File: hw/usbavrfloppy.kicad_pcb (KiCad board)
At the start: 2 copper layers, 96.5 x 70.5 mm, 67 parts, among them CON1 CONN_02X03, J1 bothdrv, J2 floppy_conn, J3 floppy_power, J5 USB_B, J6 PWRIN, J7 USB_OTG, P1 CONN_01X03, P2 CONN_01X01, P3 CONN_01X01, P4 CONN_01X01, P5 CONN_01X01, Q1 BSS138, Q10 BSS138, Q2 BSS138, Q3 BSS138, Q4 BSS138, Q5 BSS138, Q6 BSS138, Q7 BSS138, Q8 BSS138, Q9 BSS138, SW1 ~mRESET, U1 ATMEGA88-A, U2 FT232RL, Y1 16MHz

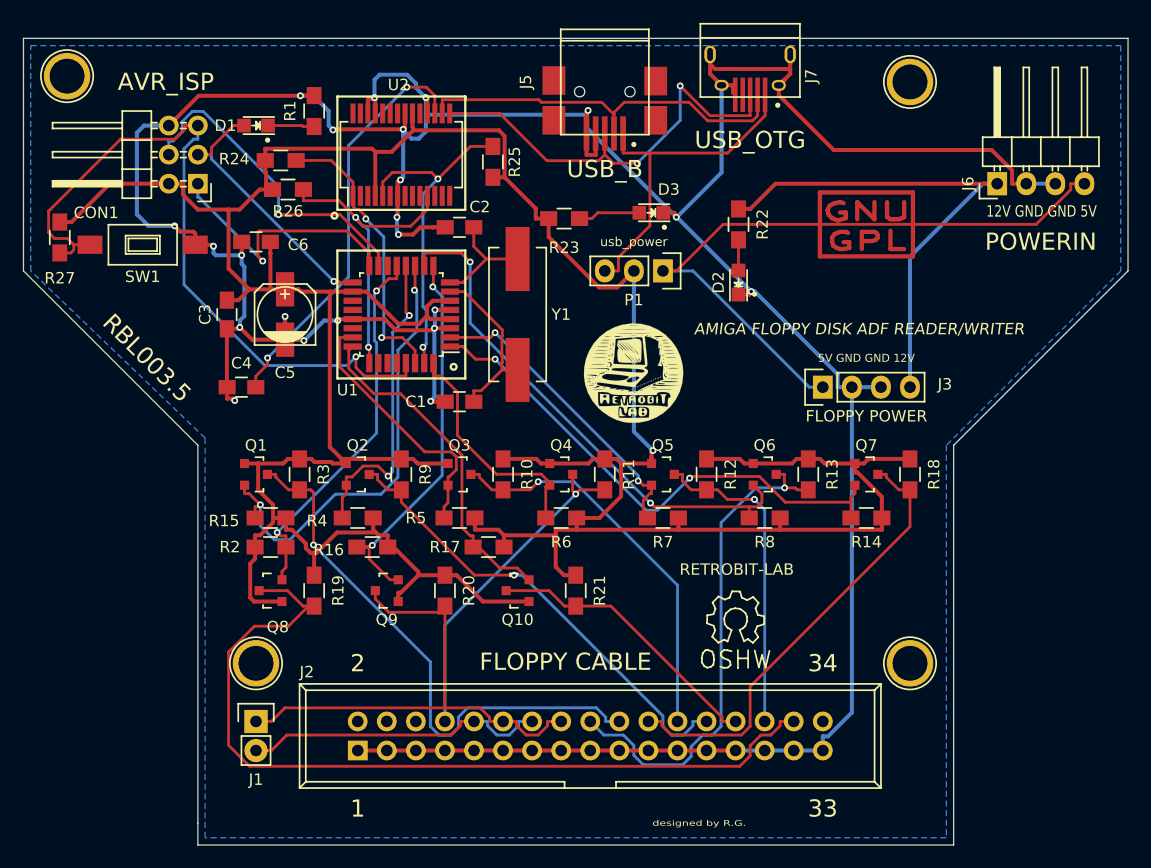
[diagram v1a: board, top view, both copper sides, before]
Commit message: Modified for new 3d components and logos
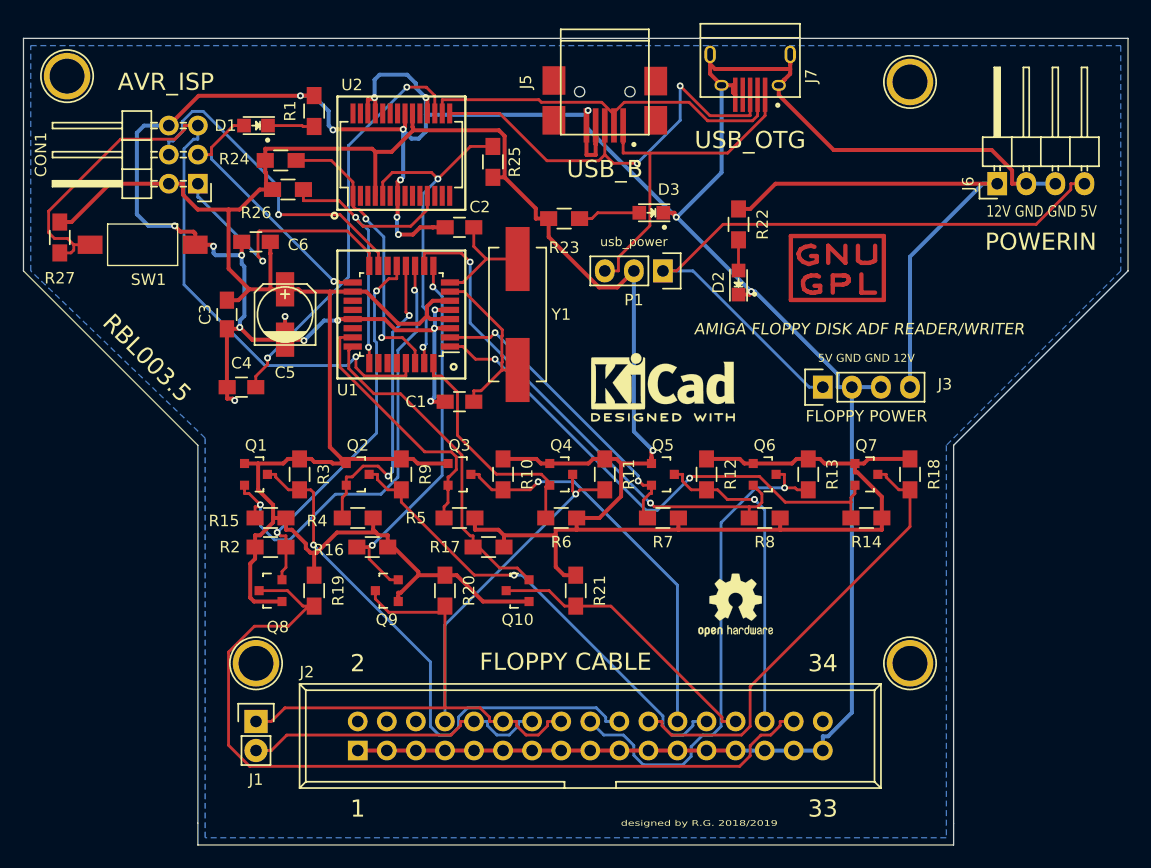
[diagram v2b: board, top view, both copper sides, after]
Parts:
- removed GNULOGO: Symbol_GNU-GPL_CopperTop_Small, Symbols:Symbol_GNU-GPL_CopperTop_Small
- removed LOGO: LOGO, RetroBitLab:amigaLogo_BW_31x12mm-SilkScreenBack
- removed LOGO2: LOGO, RetroBitLab:amigaWorkBench1-SIlkScreenBack
- removed RETROBIT-LAB: Symbol_OSHW-Logo_SilkScreen, Symbols:Symbol_OSHW-Logo_SilkScreen
- removed RETROBITLAB: LOGO, kicad-footprints:RetroBitLab_10x10
- added AMIGA: LOGO, RetroBitLab:amigaLogo_BW_31x12mm-SilkScreenBack, B.Cu at (152.4, 97.8)
- added KICAD: KiCad-Logo2_5mm_SilkScreen, Symbol:KiCad-Logo2_5mm_SilkScreen, F.Cu at (160.0, 88.9)
- added OSHW: OSHW-Logo2_7.3x6mm_SilkScreen, Symbol:OSHW-Logo2_7.3x6mm_SilkScreen, F.Cu at (166.4, 108.0)
- added REF**: Symbol_GNU-GPL_CopperTop_Small, Symbols:Symbol_GNU-GPL_CopperTop_Small, F.Cu at (175.3, 78.7)
- added WB: LOGO, RetroBitLab:amigaWorkBench1-SIlkScreenBack, B.Cu at (172.7, 76.2)
- SW1: footprint Buttons_Switches_SMD:SW_SPST_FSMSM -> RetroBitLab:SW_SPST_FSMSM_3D
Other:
- board text added: "designed by R.G. 2018/2019"
- board text removed: "designed by R.G."

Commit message: added filled zone top
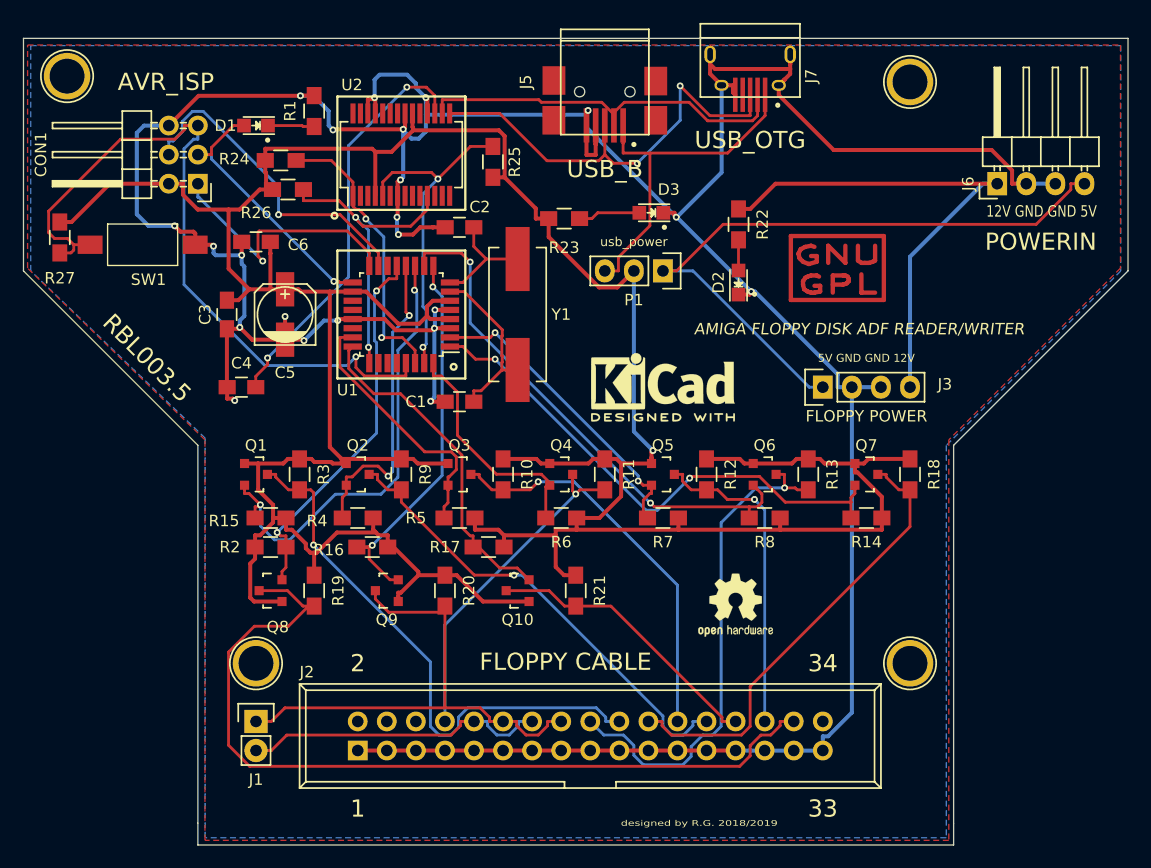
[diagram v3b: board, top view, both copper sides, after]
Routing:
- added copper zone on F.Cu, net GND
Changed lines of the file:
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@@
+    )
+  )
+  (zone (net 1) (net_name GND) (layer F.Cu) (hatch edge 0.508)
+    (connect_pads (clearance 0.508))
+    (min_thickness 0.254)
+    (fill yes (arc_segments 16) (thermal_gap 0.508) (thermal_bridge_width 0.508))
+    (polygon
+      (pts
+        (xy 200 78.5) (xy 185 93.5) (xy 185 128.5) (xy 120 128.5) (xy 120 93.5)
+        (xy 104.5 78.5) (xy 104.5 59) (xy 200 59) (xy 200 78.5)
+      )
     )
   )

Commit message: Added footprint for idc connector
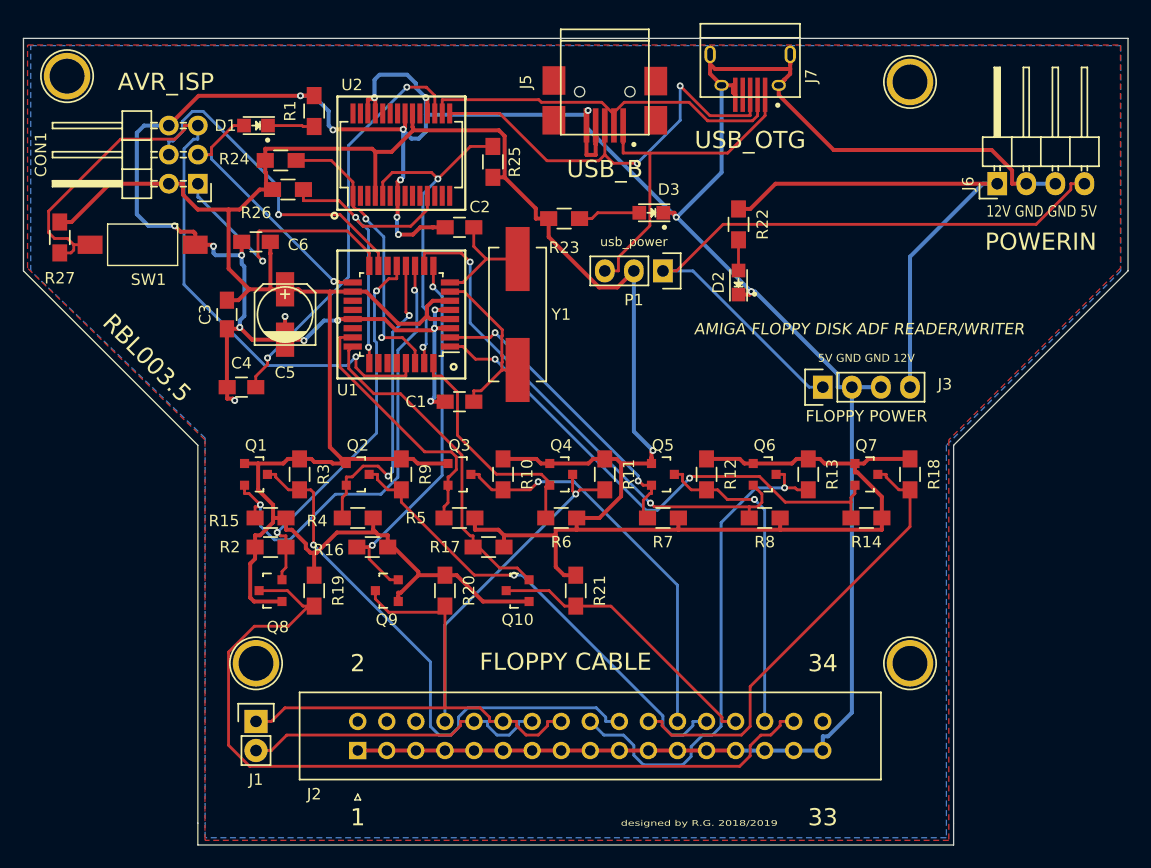
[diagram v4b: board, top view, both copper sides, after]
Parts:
- removed AMIGA: LOGO, RetroBitLab:amigaLogo_BW_31x12mm-SilkScreenBack
- removed KICAD: KiCad-Logo2_5mm_SilkScreen, Symbol:KiCad-Logo2_5mm_SilkScreen
- removed OSHW: OSHW-Logo2_7.3x6mm_SilkScreen, Symbol:OSHW-Logo2_7.3x6mm_SilkScreen
- removed REF**: Symbol_GNU-GPL_CopperTop_Small, Symbols:Symbol_GNU-GPL_CopperTop_Small
- removed WB: LOGO, RetroBitLab:amigaWorkBench1-SIlkScreenBack
- added G***: LOGO, RetroBitLab:amigaLogo_BW_31x12mm-SilkScreenBack, B.Cu at (154.9, 99.1)
- added G***: LOGO, RetroBitLab:amigaWorkBench1-SIlkScreenBack, B.Cu at (134.6, 78.7)
- J2: footprint Connect:IDC_Header_Straight_34pins -> RetroBitLab:IDC-Header_2x17_P2.54mm_Vertical_Lock
- turned J2 to 90 degrees

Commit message: Changed from 0603/0806 to 1208
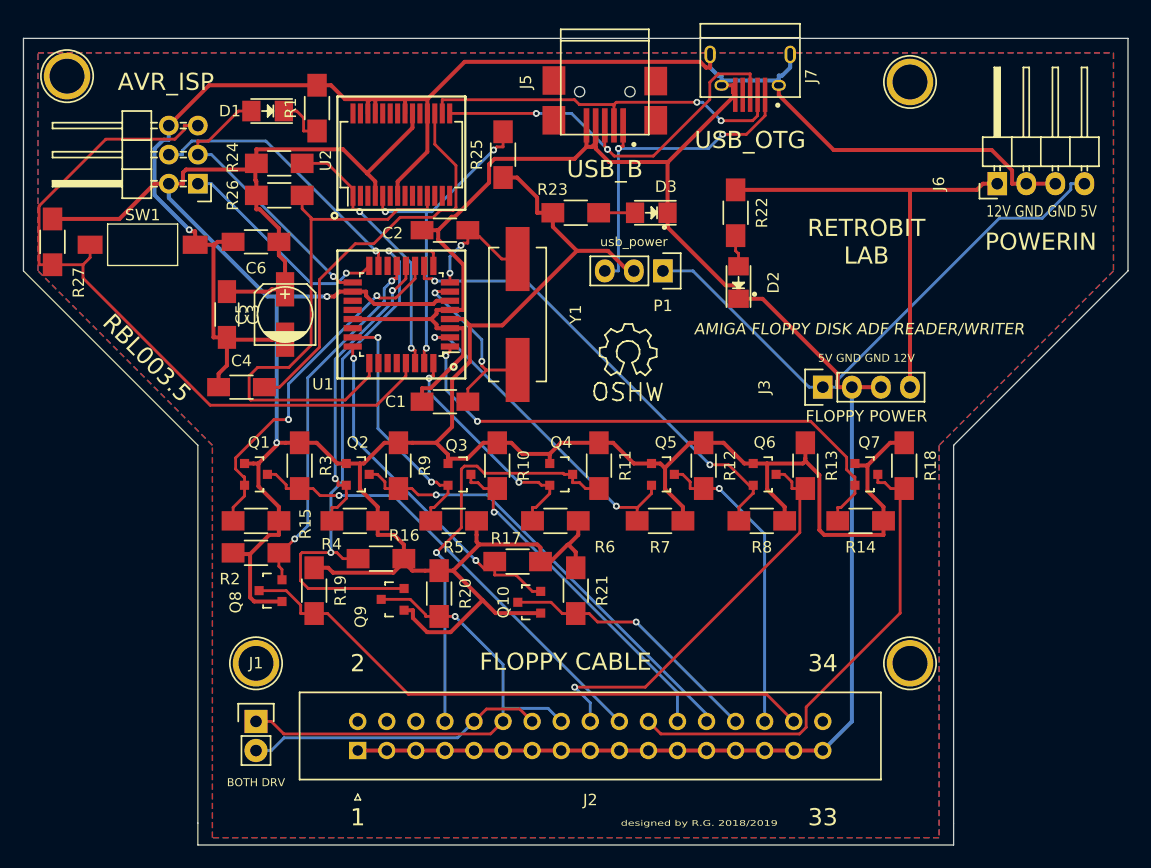
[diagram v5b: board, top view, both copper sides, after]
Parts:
- added OSHW: Symbol_OSHW-Logo_SilkScreen, Symbols:Symbol_OSHW-Logo_SilkScreen, F.Cu at (157.0, 85.9)
- C1, C2, C3, C4, C6: footprint Capacitors_SMD:C_0805_HandSoldering -> Capacitors_SMD:C_1206_HandSoldering
- D1, D2, D3: footprint LEDs:LED_0805 -> LEDs:LED_1206
- R1, R10, R11, R12, R13, R14, R15, R16, R17, R18, R19, R2, R20, R21, R22, R23, R24, R25, R26, R27, R3, R4, R5, R6, R7, R8, R9: footprint Resistors_SMD:R_0805_HandSoldering -> Resistors_SMD:R_1206_HandSoldering
- moved R17 2.84 mm to (147.3, 104.1)
- moved LOGO 1.80 mm to (153.7, 97.8)
- moved D1 1.63 mm to (125.5, 64.8)
- moved Q10 1.44 mm to (148.3, 107.7)
- moved R15 1.37 mm to (124.5, 103.4)
- moved R2 1.30 mm to (124.5, 100.6)
- moved C2 1.30 mm to (141.0, 75.2)
- moved C1 1.27 mm to (141.0, 90.2)
- moved R16 1.27 mm to (135.4, 103.9)
- moved R23 1.14 mm to (152.4, 73.7)
- moved R25 1.09 mm to (146.1, 68.6)
- moved R22 1.05 mm to (166.4, 73.7)
- moved R10 0.92 mm to (145.5, 95.8)
- moved R11 0.92 mm to (154.4, 95.8)
- moved R18 0.92 mm to (181.1, 95.8)
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- renumbered G*** to LOGO, G*** to WB
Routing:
- net /~SIDE1: track 74.7 -> 51.9 mm
- net /CTS: track 27.9 -> 46.2 mm, vias 2 -> 0
- net /~mMOTEN: track 34.1 -> 51.3 mm
- net Vcc_FLOPPY: track 308.1 -> 318.4 mm, vias 1 -> 2
- net VCC: track 58.5 -> 49.0 mm
- net /~mSTEP: track 40.3 -> 31.6 mm
- net /~STEP: track 48.5 -> 39.9 mm
- net /~DIR: track 44.1 -> 36.1 mm
- net GND: track 323.4 -> 316.1 mm, vias 22 -> 1
- net /~INDEX: track 29.8 -> 36.6 mm
- net /~mDIR: track 46.4 -> 41.2 mm
- net +12V: track 45.2 -> 40.3 mm
- net /MOSI: track 28.8 -> 24.2 mm
- net /~WGATE: track 34.7 -> 30.4 mm
- net /MISO: track 23.5 -> 19.3 mm
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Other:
- board text added: "BOTH DRV"
- board text added: "RETROBIT LAB"
